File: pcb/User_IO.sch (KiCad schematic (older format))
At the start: 17 parts

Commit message: Added part numbers and updated schematic
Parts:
- gave numbers to parts that had none: 17
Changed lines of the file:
@@
 $EndDescr
 $Comp
-L XC7Axxt-FGG484 U?
+L XC7Axxt-FGG484 U401
 U 5 1 565FC0A5
 P 3400 3950
-F 0 "U?" H 2500 1350 60  0000 C CNN
+F 0 "U401" H 2500 1350 60  0000 C CNN
 F 1 "XC7Axxt-FGG484" H 2800 6550 60  0000 C CNN
 F 2 "" H 3400 4000 60  0000 C CNN
@@
 $EndComp
 $Comp
-L LED D?
+L LED D1201
 U 1 1 565FC0D4
 P 6800 1600
-F 0 "D?" H 6800 1700 50  0000 C CNN
+F 0 "D1201" H 6800 1700 50  0000 C CNN
 F 1 "LED" H 6800 1500 50  0000 C CNN
 F 2 "" H 6800 1600 60  0000 C CNN
@@
 $EndComp
 $Comp
-L LED D?
+L LED D1202
 U 1 1 565FC10C
 P 6800 1900
-F 0 "D?" H 6800 2000 50  0000 C CNN
+F 0 "D1202" H 6800 2000 50  0000 C CNN
 F 1 "LED" H 6800 1800 50  0000 C CNN
 F 2 "" H 6800 1900 60  0000 C CNN
@@
 $EndComp
 $Comp
-L LED D?
+L LED D1203
 U 1 1 565FC132
 P 6800 2200
-F 0 "D?" H 6800 2300 50  0000 C CNN
+F 0 "D1203" H 6800 2300 50  0000 C CNN
 F 1 "LED" H 6800 2100 50  0000 C CNN
 F 2 "" H 6800 2200 60  0000 C CNN
@@
 $EndComp
 $Comp
-L LED D?
+L LED D1204
 U 1 1 565FC15A
 P 6800 2500
-F 0 "D?" H 6800 2600 50  0000 C CNN
+F 0 "D1204" H 6800 2600 50  0000 C CNN
 F 1 "LED" H 6800 2400 50  0000 C CNN
 F 2 "" H 6800 2500 60  0000 C CNN
@@
 $EndComp
 $Comp
-L R R?
+L R R1201
 U 1 1 565FC21B
 P 6350 1600
-F 0 "R?" V 6430 1600 50  0000 C CNN
+F 0 "R1201" V 6430 1600 50  0000 C CNN
 F 1 "R" V 6350 1600 50  0000 C CNN
 F 2 "" V 6280 1600 30  0000 C CNN
@@
 $EndComp
 $Comp
-L R R?
+L R R1202
 U 1 1 565FC251
 P 6350 1900
-F 0 "R?" V 6430 1900 50  0000 C CNN
+F 0 "R1202" V 6430 1900 50  0000 C CNN
 F 1 "R" V 6350 1900 50  0000 C CNN
 F 2 "" V 6280 1900 30  0000 C CNN
@@
 $EndComp
 $Comp
-L R R?
+L R R1203
 U 1 1 565FC282
 P 6350 2200
-F 0 "R?" V 6430 2200 50  0000 C CNN
+F 0 "R1203" V 6430 2200 50  0000 C CNN
 F 1 "R" V 6350 2200 50  0000 C CNN
 F 2 "" V 6280 2200 30  0000 C CNN
@@
 $EndComp
 $Comp
-L R R?
+L R R1204
 U 1 1 565FC2C2
 P 6350 2500
-F 0 "R?" V 6430 2500 50  0000 C CNN
+F 0 "R1204" V 6430 2500 50  0000 C CNN
 F 1 "R" V 6350 2500 50  0000 C CNN
 F 2 "" V 6280 2500 30  0000 C CNN
@@
 $EndComp
 $Comp
-L GND #PWR?
+L GND #PWR1203
 U 1 1 565FC384
 P 7100 2600
-F 0 "#PWR?" H 7100 2350 50  0001 C CNN
+F 0 "#PWR1203" H 7100 2350 50  0001 C CNN
 F 1 "GND" H 7100 2450 50  0000 C CNN
 F 2 "" H 7100 2600 60  0000 C CNN
@@
 $EndComp
 $Comp
-L CONN_02X05 P?
+L CONN_02X05 P1201
 U 1 1 565FC541
 P 8050 3300
-F 0 "P?" H 8050 3600 50  0000 C CNN
+F 0 "P1201" H 8050 3600 50  0000 C CNN
 F 1 "CONN_02X05" H 8050 3000 50  0000 C CNN
 F 2 "" H 8050 2100 60  0000 C CNN
@@
 $EndComp
 $Comp
-L CONN_02X05 P?
+L CONN_02X05 P1202
 U 1 1 565FC5D6
 P 8050 4200
-F 0 "P?" H 8050 4500 50  0000 C CNN
+F 0 "P1202" H 8050 4500 50  0000 C CNN
 F 1 "CONN_02X05" H 8050 3900 50  0000 C CNN
 F 2 "" H 8050 3000 60  0000 C CNN
@@
 IO15
 $Comp
-L GND #PWR?
+L GND #PWR1206
 U 1 1 565FD605
 P 8500 3600
-F 0 "#PWR?" H 8500 3350 50  0001 C CNN
+F 0 "#PWR1206" H 8500 3350 50  0001 C CNN
 F 1 "GND" H 8500 3450 50  0000 C CNN
 F 2 "" H 8500 3600 60  0000 C CNN
@@
 $EndComp
 $Comp
-L GND #PWR?
+L GND #PWR1207
 U 1 1 565FD63A
 P 8500 4500
-F 0 "#PWR?" H 8500 4250 50  0001 C CNN
+F 0 "#PWR1207" H 8500 4250 50  0001 C CNN
 F 1 "GND" H 8500 4350 50  0000 C CNN
 F 2 "" H 8500 4500 60  0000 C CNN
@@
 $EndComp
 $Comp
-L +3V3 #PWR?
+L +3V3 #PWR1204
 U 1 1 565FD72A
 P 7600 3600
-F 0 "#PWR?" H 7600 3450 50  0001 C CNN
+F 0 "#PWR1204" H 7600 3450 50  0001 C CNN
 F 1 "+3V3" H 7600 3740 50  0000 C CNN
 F 2 "" H 7600 3600 60  0000 C CNN
@@
 $EndComp
 $Comp
-L +3V3 #PWR?
+L +3V3 #PWR1205
 U 1 1 565FD75F
 P 7600 4500
-F 0 "#PWR?" H 7600 4350 50  0001 C CNN
+F 0 "#PWR1205" H 7600 4350 50  0001 C CNN
 F 1 "+3V3" H 7600 4640 50  0000 C CNN
 F 2 "" H 7600 4500 60  0000 C CNN
@@
 	7600 4400 7600 4500
 $Comp
-L SW_PUSH SW?
+L SW_PUSH SW1202
 U 1 1 565FD8DE
 P 10300 3400
-F 0 "SW?" H 10450 3510 50  0000 C CNN
+F 0 "SW1202" H 10450 3510 50  0000 C CNN
 F 1 "SW_PUSH" H 10300 3320 50  0000 C CNN
 F 2 "" H 10300 3400 60  0000 C CNN
@@
 $EndComp
 $Comp
-L SW_PUSH SW?
+L SW_PUSH SW1201
 U 1 1 565FD92F
 P 10000 3400
-F 0 "SW?" H 10150 3510 50  0000 C CNN
+F 0 "SW1201" H 10150 3510 50  0000 C CNN
 F 1 "SW_PUSH" H 10000 3320 50  0000 C CNN
 F 2 "" H 10000 3400 60  0000 C CNN
@@
 $EndComp
 $Comp
-L R R?
+L R R1208
 U 1 1 565FD996
 P 10300 2750
-F 0 "R?" V 10380 2750 50  0000 C CNN
+F 0 "R1208" V 10380 2750 50  0000 C CNN
 F 1 "R" V 10300 2750 50  0000 C CNN
 F 2 "" V 10230 2750 30  0000 C CNN
@@
 $EndComp
 $Comp
-L R R?
+L R R1207
 U 1 1 565FD9E8
 P 10000 2750
-F 0 "R?" V 10080 2750 50  0000 C CNN
+F 0 "R1207" V 10080 2750 50  0000 C CNN
 F 1 "R" V 10000 2750 50  0000 C CNN
 F 2 "" V 9930 2750 30  0000 C CNN
@@
 $EndComp
 $Comp
-L +3V3 #PWR?
+L +3V3 #PWR1208
 U 1 1 565FDB4D
 P 10000 2400
-F 0 "#PWR?" H 10000 2250 50  0001 C CNN
+F 0 "#PWR1208" H 10000 2250 50  0001 C CNN
 F 1 "+3V3" H 10000 2540 50  0000 C CNN
 F 2 "" H 10000 2400 60  0000 C CNN
@@
 $EndComp
 $Comp
-L GND #PWR?
+L GND #PWR1209
 U 1 1 565FDBBB
 P 10000 3900
-F 0 "#PWR?" H 10000 3650 50  0001 C CNN
+F 0 "#PWR1209" H 10000 3650 50  0001 C CNN
 F 1 "GND" H 10000 3750 50  0000 C CNN
 F 2 "" H 10000 3900 60  0000 C CNN
@@
 SFP_SCL
 $Comp
-L R R?
+L R R1205
 U 1 1 566081C8
 P 6500 4950
-F 0 "R?" V 6580 4950 50  0000 C CNN
+F 0 "R1205" V 6580 4950 50  0000 C CNN
 F 1 "R" V 6500 4950 50  0000 C CNN
 F 2 "" V 6430 4950 30  0000 C CNN
@@
 $EndComp
 $Comp
-L R R?
+L R R1206
 U 1 1 5660821E
 P 6500 5750
-F 0 "R?" V 6580 5750 50  0000 C CNN
+F 0 "R1206" V 6580 5750 50  0000 C CNN
 F 1 "R" V 6500 5750 50  0000 C CNN
 F 2 "" V 6430 5750 30  0000 C CNN
@@
 $EndComp
 $Comp
-L +3V3 #PWR?
+L +3V3 #PWR1201
 U 1 1 56608307
 P 6500 4700
-F 0 "#PWR?" H 6500 4550 50  0001 C CNN
+F 0 "#PWR1201" H 6500 4550 50  0001 C CNN
 F 1 "+3V3" H 6500 4840 50  0000 C CNN
 F 2 "" H 6500 4700 60  0000 C CNN
@@
 $EndComp
 $Comp
-L +3V3 #PWR?
+L +3V3 #PWR1202
 U 1 1 5660834E
 P 6500 5500
-F 0 "#PWR?" H 6500 5350 50  0001 C CNN
+F 0 "#PWR1202" H 6500 5350 50  0001 C CNN
 F 1 "+3V3" H 6500 5640 50  0000 C CNN
 F 2 "" H 6500 5500 60  0000 C CNN

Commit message: mostly done with component placement
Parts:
- D1201, D1202, D1203, D1204: footprint (none) -> LEDs:LED-0805
- P1201, P1202: footprint (none) -> Pin_Headers:Pin_Header_Straight_2x05
- R1201, R1202, R1203, R1204, R1205, R1206, R1207, R1208: footprint (none) -> wbraun_smd:R_0402
- SW1201, SW1202: footprint (none) -> wbraun_smd:button-5mm
- U401: footprint (none) -> wbraun_smd:BGA_484_22x22_FULLARRAY_1MM
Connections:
- net +3V3: now also R1206.1
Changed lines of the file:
@@
 F 0 "U401" H 2500 1350 60  0000 C CNN
 F 1 "XC7Axxt-FGG484" H 2800 6550 60  0000 C CNN
-F 2 "" H 3400 4000 60  0000 C CNN
+F 2 "wbraun_smd:BGA_484_22x22_FULLARRAY_1MM" H 3400 4000 60  0001 C CNN
 F 3 "" H 3400 4000 60  0000 C CNN
 	5    3400 3950
@@
 F 0 "D1201" H 6800 1700 50  0000 C CNN
 F 1 "LED" H 6800 1500 50  0000 C CNN
-F 2 "" H 6800 1600 60  0000 C CNN
+F 2 "LEDs:LED-0805" H 6800 1600 60  0001 C CNN
 F 3 "" H 6800 1600 60  0000 C CNN
 	1    6800 1600
@@
 F 0 "D1202" H 6800 2000 50  0000 C CNN
 F 1 "LED" H 6800 1800 50  0000 C CNN
-F 2 "" H 6800 1900 60  0000 C CNN
+F 2 "LEDs:LED-0805" H 6800 1900 60  0001 C CNN
 F 3 "" H 6800 1900 60  0000 C CNN
 	1    6800 1900
@@
 F 0 "D1203" H 6800 2300 50  0000 C CNN
 F 1 "LED" H 6800 2100 50  0000 C CNN
-F 2 "" H 6800 2200 60  0000 C CNN
+F 2 "LEDs:LED-0805" H 6800 2200 60  0001 C CNN
 F 3 "" H 6800 2200 60  0000 C CNN
 	1    6800 2200
@@
 F 0 "D1204" H 6800 2600 50  0000 C CNN
 F 1 "LED" H 6800 2400 50  0000 C CNN
-F 2 "" H 6800 2500 60  0000 C CNN
+F 2 "LEDs:LED-0805" H 6800 2500 60  0001 C CNN
 F 3 "" H 6800 2500 60  0000 C CNN
 	1    6800 2500
@@
 F 0 "R1201" V 6430 1600 50  0000 C CNN
 F 1 "R" V 6350 1600 50  0000 C CNN
-F 2 "" V 6280 1600 30  0000 C CNN
+F 2 "wbraun_smd:R_0402" V 6280 1600 30  0001 C CNN
 F 3 "" H 6350 1600 30  0000 C CNN
 	1    6350 1600
@@
 F 0 "R1202" V 6430 1900 50  0000 C CNN
 F 1 "R" V 6350 1900 50  0000 C CNN
-F 2 "" V 6280 1900 30  0000 C CNN
+F 2 "wbraun_smd:R_0402" V 6280 1900 30  0001 C CNN
 F 3 "" H 6350 1900 30  0000 C CNN
 	1    6350 1900
@@
 F 0 "R1203" V 6430 2200 50  0000 C CNN
 F 1 "R" V 6350 2200 50  0000 C CNN
-F 2 "" V 6280 2200 30  0000 C CNN
+F 2 "wbraun_smd:R_0402" V 6280 2200 30  0001 C CNN
 F 3 "" H 6350 2200 30  0000 C CNN
 	1    6350 2200
@@
 F 0 "R1204" V 6430 2500 50  0000 C CNN
 F 1 "R" V 6350 2500 50  0000 C CNN
-F 2 "" V 6280 2500 30  0000 C CNN
+F 2 "wbraun_smd:R_0402" V 6280 2500 30  0001 C CNN
 F 3 "" H 6350 2500 30  0000 C CNN
 	1    6350 2500
@@
 $EndComp
 $Comp
-L GND #PWR1203
+L GND #PWR0165
 U 1 1 565FC384
 P 7100 2600
-F 0 "#PWR1203" H 7100 2350 50  0001 C CNN
+F 0 "#PWR0165" H 7100 2350 50  0001 C CNN
 F 1 "GND" H 7100 2450 50  0000 C CNN
 F 2 "" H 7100 2600 60  0000 C CNN
@@
 F 0 "P1201" H 8050 3600 50  0000 C CNN
 F 1 "CONN_02X05" H 8050 3000 50  0000 C CNN
-F 2 "" H 8050 2100 60  0000 C CNN
+F 2 "Pin_Headers:Pin_Header_Straight_2x05" H 8050 2100 60  0001 C CNN
 F 3 "" H 8050 2100 60  0000 C CNN
 	1    8050 3300
@@
 F 0 "P1202" H 8050 4500 50  0000 C CNN
 F 1 "CONN_02X05" H 8050 3900 50  0000 C CNN
-F 2 "" H 8050 3000 60  0000 C CNN
+F 2 "Pin_Headers:Pin_Header_Straight_2x05" H 8050 3000 60  0001 C CNN
 F 3 "" H 8050 3000 60  0000 C CNN
 	1    8050 4200
@@
 IO15
 $Comp
-L GND #PWR1206
+L GND #PWR0166
 U 1 1 565FD605
 P 8500 3600
-F 0 "#PWR1206" H 8500 3350 50  0001 C CNN
+F 0 "#PWR0166" H 8500 3350 50  0001 C CNN
 F 1 "GND" H 8500 3450 50  0000 C CNN
 F 2 "" H 8500 3600 60  0000 C CNN
@@
 $EndComp
 $Comp
-L GND #PWR1207
+L GND #PWR0167
 U 1 1 565FD63A
 P 8500 4500
-F 0 "#PWR1207" H 8500 4250 50  0001 C CNN
+F 0 "#PWR0167" H 8500 4250 50  0001 C CNN
 F 1 "GND" H 8500 4350 50  0000 C CNN
 F 2 "" H 8500 4500 60  0000 C CNN
@@
 $EndComp
 $Comp
-L +3V3 #PWR1204
+L +3V3 #PWR0168
 U 1 1 565FD72A
 P 7600 3600
-F 0 "#PWR1204" H 7600 3450 50  0001 C CNN
+F 0 "#PWR0168" H 7600 3450 50  0001 C CNN
 F 1 "+3V3" H 7600 3740 50  0000 C CNN
 F 2 "" H 7600 3600 60  0000 C CNN
@@
 $EndComp
 $Comp
-L +3V3 #PWR1205
+L +3V3 #PWR0169
 U 1 1 565FD75F
 P 7600 4500
-F 0 "#PWR1205" H 7600 4350 50  0001 C CNN
+F 0 "#PWR0169" H 7600 4350 50  0001 C CNN
 F 1 "+3V3" H 7600 4640 50  0000 C CNN
 F 2 "" H 7600 4500 60  0000 C CNN
@@
 F 0 "SW1202" H 10450 3510 50  0000 C CNN
 F 1 "SW_PUSH" H 10300 3320 50  0000 C CNN
-F 2 "" H 10300 3400 60  0000 C CNN
+F 2 "wbraun_smd:button-5mm" H 10300 3400 60  0001 C CNN
 F 3 "" H 10300 3400 60  0000 C CNN
 	1    10300 3400
@@
 F 0 "SW1201" H 10150 3510 50  0000 C CNN
 F 1 "SW_PUSH" H 10000 3320 50  0000 C CNN
-F 2 "" H 10000 3400 60  0000 C CNN
+F 2 "wbraun_smd:button-5mm" H 10000 3400 60  0001 C CNN
 F 3 "" H 10000 3400 60  0000 C CNN
 	1    10000 3400
@@
 F 0 "R1208" V 10380 2750 50  0000 C CNN
 F 1 "R" V 10300 2750 50  0000 C CNN
-F 2 "" V 10230 2750 30  0000 C CNN
+F 2 "wbraun_smd:R_0402" V 10230 2750 30  0001 C CNN
 F 3 "" H 10300 2750 30  0000 C CNN
 	1    10300 2750
@@
 F 0 "R1207" V 10080 2750 50  0000 C CNN
 F 1 "R" V 10000 2750 50  0000 C CNN
-F 2 "" V 9930 2750 30  0000 C CNN
+F 2 "wbraun_smd:R_0402" V 9930 2750 30  0001 C CNN
 F 3 "" H 10000 2750 30  0000 C CNN
 	1    10000 2750
@@
 $EndComp
 $Comp
-L +3V3 #PWR1208
+L +3V3 #PWR0170
 U 1 1 565FDB4D
 P 10000 2400
-F 0 "#PWR1208" H 10000 2250 50  0001 C CNN
+F 0 "#PWR0170" H 10000 2250 50  0001 C CNN
 F 1 "+3V3" H 10000 2540 50  0000 C CNN
 F 2 "" H 10000 2400 60  0000 C CNN
@@
 $EndComp
 $Comp
-L GND #PWR1209
+L GND #PWR0171
 U 1 1 565FDBBB
 P 10000 3900
-F 0 "#PWR1209" H 10000 3650 50  0001 C CNN
+F 0 "#PWR0171" H 10000 3650 50  0001 C CNN
 F 1 "GND" H 10000 3750 50  0000 C CNN
 F 2 "" H 10000 3900 60  0000 C CNN
@@
 F 0 "R1205" V 6580 4950 50  0000 C CNN
 F 1 "R" V 6500 4950 50  0000 C CNN
-F 2 "" V 6430 4950 30  0000 C CNN
+F 2 "wbraun_smd:R_0402" V 6430 4950 30  0001 C CNN
 F 3 "" H 6500 4950 30  0000 C CNN
 	1    6500 4950
@@
 F 0 "R1206" V 6580 5750 50  0000 C CNN
 F 1 "R" V 6500 5750 50  0000 C CNN
-F 2 "" V 6430 5750 30  0000 C CNN
+F 2 "wbraun_smd:R_0402" V 6430 5750 30  0001 C CNN
 F 3 "" H 6500 5750 30  0000 C CNN
 	1    6500 5750
@@
 $EndComp
 $Comp
-L +3V3 #PWR1201
+L +3V3 #PWR0172
 U 1 1 56608307
 P 6500 4700
-F 0 "#PWR1201" H 6500 4550 50  0001 C CNN
+F 0 "#PWR0172" H 6500 4550 50  0001 C CNN
 F 1 "+3V3" H 6500 4840 50  0000 C CNN
 F 2 "" H 6500 4700 60  0000 C CNN
@@
 $EndComp
 $Comp
-L +3V3 #PWR1202
+L +3V3 #PWR0173
 U 1 1 5660834E
 P 6500 5500
-F 0 "#PWR1202" H 6500 5350 50  0001 C CNN
+F 0 "#PWR0173" H 6500 5350 50  0001 C CNN
 F 1 "+3V3" H 6500 5640 50  0000 C CNN
 F 2 "" H 6500 5500 60  0000 C CNN
@@
 Text HLabel 8100 5900 2    60   Input ~ 0
 PCIE_PERST
+Wire Wire Line
+	6500 5500 6500 5600
 $EndSCHEMATC

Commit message: Finished initial component placement
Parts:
- removed R1205, R1206: R, wbraun_smd:R_0402, symbol R
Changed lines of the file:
@@
 Text Label 4700 5500 0    60   ~ 0
 SFP_SCL
-$Comp
-L R R1205
-U 1 1 566081C8
-P 6500 4950
-F 0 "R1205" V 6580 4950 50  0000 C CNN
-F 1 "R" V 6500 4950 50  0000 C CNN
-F 2 "wbraun_smd:R_0402" V 6430 4950 30  0001 C CNN
-F 3 "" H 6500 4950 30  0000 C CNN
-	1    6500 4950
-	1    0    0    -1
-$EndComp
-$Comp
-L R R1206
-U 1 1 5660821E
-P 6500 5750
-F 0 "R1206" V 6580 5750 50  0000 C CNN
-F 1 "R" V 6500 5750 50  0000 C CNN
-F 2 "wbraun_smd:R_0402" V 6430 5750 30  0001 C CNN
-F 3 "" H 6500 5750 30  0000 C CNN
-	1    6500 5750
-	1    0    0    -1
-$EndComp
-$Comp
-L +3V3 #PWR0172
-U 1 1 56608307
-P 6500 4700
-F 0 "#PWR0172" H 6500 4550 50  0001 C CNN
-F 1 "+3V3" H 6500 4840 50  0000 C CNN
-F 2 "" H 6500 4700 60  0000 C CNN
-F 3 "" H 6500 4700 60  0000 C CNN
-	1    6500 4700
-	1    0    0    -1
-$EndComp
-$Comp
-L +3V3 #PWR0173
-U 1 1 5660834E
-P 6500 5500
-F 0 "#PWR0173" H 6500 5350 50  0001 C CNN
-F 1 "+3V3" H 6500 5640 50  0000 C CNN
-F 2 "" H 6500 5500 60  0000 C CNN
-F 3 "" H 6500 5500 60  0000 C CNN
-	1    6500 5500
-	1    0    0    -1
-$EndComp
-Wire Wire Line
-	6500 4700 6500 4800
-Wire Wire Line
-	6300 5100 6700 5100
-Connection ~ 6500 5100
-Wire Wire Line
-	6300 5900 6700 5900
-Connection ~ 6500 5900
 Wire Wire Line
 	7700 5300 8100 5300
@@
 PCIE_PERST
 Wire Wire Line
-	6500 5500 6500 5600
+	6300 5100 6700 5100
+Wire Wire Line
+	6300 5900 6700 5900
 $EndSCHEMATC

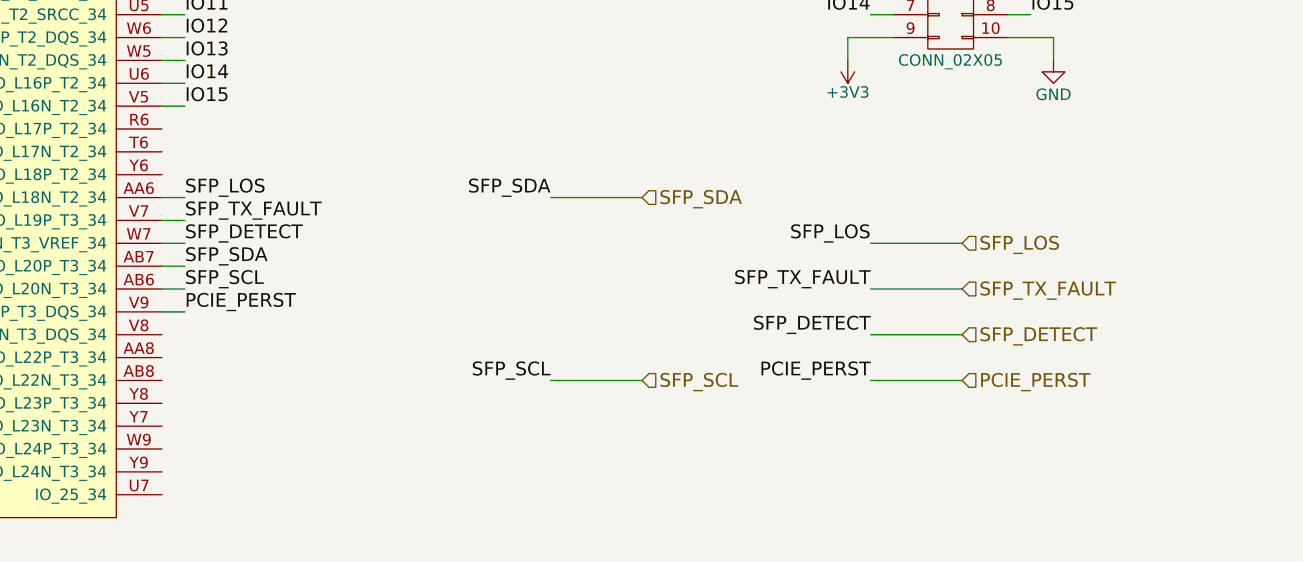
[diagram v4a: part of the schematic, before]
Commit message: Finished most of the routing, removed DDR-3
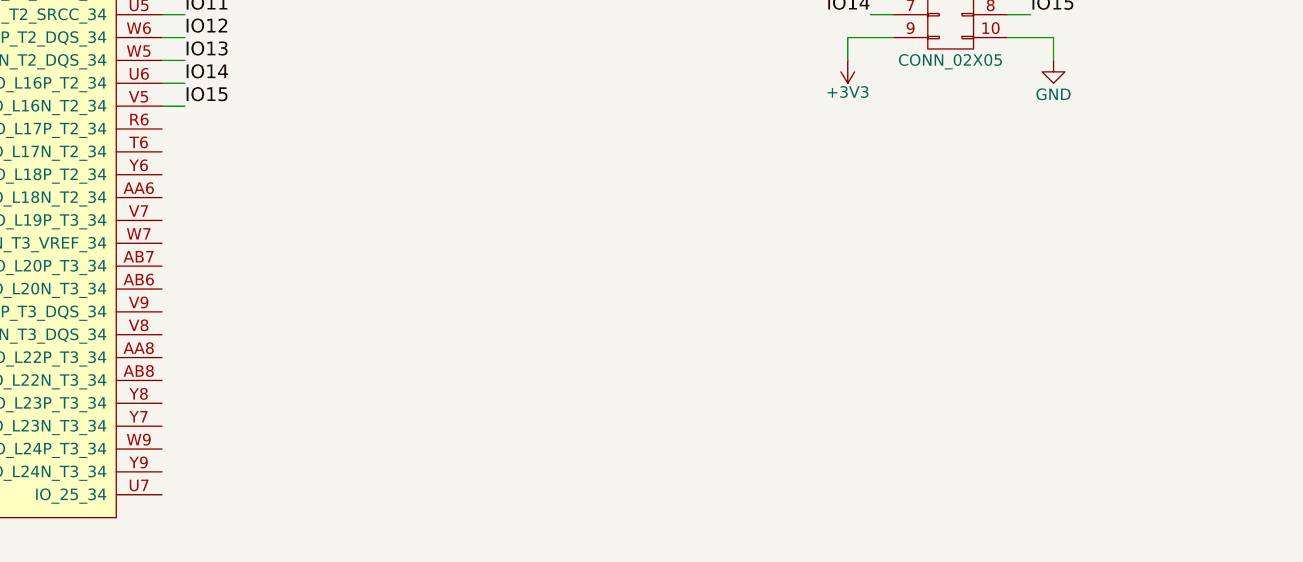
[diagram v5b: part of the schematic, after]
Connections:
- net PCIE_PERST: no longer names the net of U401.V9 (IO_L21P_T3_DQS_34)
- net SFP_DETECT: no longer names the net of U401.W7 (IO_L19N_T3_VREF_34)
- net SFP_LOS: no longer names the net of U401.AA6 (IO_L18N_T2_34)
- net SFP_SCL: no longer names the net of U401.AB6 (IO_L20N_T3_34)
- net SFP_SDA: no longer names the net of U401.AB7 (IO_L20P_T3_34)
- net SFP_TX_FAULT: no longer names the net of U401.V7 (IO_L19P_T3_34)
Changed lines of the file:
@@
 $Descr A4 11693 8268
 encoding utf-8
-Sheet 12 13
+Sheet 12 11
 Title ""
 Date ""
@@
 $EndComp
 $Comp
-L GND #PWR0165
+L GND #PWR0156
 U 1 1 565FC384
 P 7100 2600
-F 0 "#PWR0165" H 7100 2350 50  0001 C CNN
+F 0 "#PWR0156" H 7100 2350 50  0001 C CNN
 F 1 "GND" H 7100 2450 50  0000 C CNN
 F 2 "" H 7100 2600 60  0000 C CNN
@@
 IO15
 $Comp
-L GND #PWR0166
+L GND #PWR0157
 U 1 1 565FD605
 P 8500 3600
-F 0 "#PWR0166" H 8500 3350 50  0001 C CNN
+F 0 "#PWR0157" H 8500 3350 50  0001 C CNN
 F 1 "GND" H 8500 3450 50  0000 C CNN
 F 2 "" H 8500 3600 60  0000 C CNN
@@
 $EndComp
 $Comp
-L GND #PWR0167
+L GND #PWR0158
 U 1 1 565FD63A
 P 8500 4500
-F 0 "#PWR0167" H 8500 4250 50  0001 C CNN
+F 0 "#PWR0158" H 8500 4250 50  0001 C CNN
 F 1 "GND" H 8500 4350 50  0000 C CNN
 F 2 "" H 8500 4500 60  0000 C CNN
@@
 $EndComp
 $Comp
-L +3V3 #PWR0168
+L +3V3 #PWR0159
 U 1 1 565FD72A
 P 7600 3600
-F 0 "#PWR0168" H 7600 3450 50  0001 C CNN
+F 0 "#PWR0159" H 7600 3450 50  0001 C CNN
 F 1 "+3V3" H 7600 3740 50  0000 C CNN
 F 2 "" H 7600 3600 60  0000 C CNN
@@
 $EndComp
 $Comp
-L +3V3 #PWR0169
+L +3V3 #PWR0160
 U 1 1 565FD75F
 P 7600 4500
-F 0 "#PWR0169" H 7600 4350 50  0001 C CNN
+F 0 "#PWR0160" H 7600 4350 50  0001 C CNN
 F 1 "+3V3" H 7600 4640 50  0000 C CNN
 F 2 "" H 7600 4500 60  0000 C CNN
@@
 $EndComp
 $Comp
-L +3V3 #PWR0170
+L +3V3 #PWR0161
 U 1 1 565FDB4D
 P 10000 2400
-F 0 "#PWR0170" H 10000 2250 50  0001 C CNN
+F 0 "#PWR0161" H 10000 2250 50  0001 C CNN
 F 1 "+3V3" H 10000 2540 50  0000 C CNN
 F 2 "" H 10000 2400 60  0000 C CNN
@@
 $EndComp
 $Comp
-L GND #PWR0171
+L GND #PWR0162
 U 1 1 565FDBBB
 P 10000 3900
-F 0 "#PWR0171" H 10000 3650 50  0001 C CNN
+F 0 "#PWR0162" H 10000 3650 50  0001 C CNN
 F 1 "GND" H 10000 3750 50  0000 C CNN
 F 2 "" H 10000 3900 60  0000 C CNN
@@
 Text Label 9800 3100 2    60   ~ 0
 B1
-Wire Wire Line
-	4600 5100 4700 5100
-Wire Wire Line
-	4600 5200 4700 5200
-Wire Wire Line
-	4600 5300 4700 5300
-Text Label 4700 5100 0    60   ~ 0
-SFP_LOS
-Text Label 4700 5200 0    60   ~ 0
-SFP_TX_FAULT
-Text Label 4700 5300 0    60   ~ 0
-SFP_DETECT
-Wire Wire Line
-	4600 5400 4700 5400
-Wire Wire Line
-	4600 5500 4700 5500
-Text Label 4700 5400 0    60   ~ 0
-SFP_SDA
-Text Label 4700 5500 0    60   ~ 0
-SFP_SCL
-Wire Wire Line
-	7700 5300 8100 5300
-Wire Wire Line
-	7700 5500 8100 5500
-Wire Wire Line
-	7700 5700 8100 5700
-Text Label 6300 5100 2    60   ~ 0
-SFP_SDA
-Text Label 6300 5900 2    60   ~ 0
-SFP_SCL
-Text Label 7700 5300 2    60   ~ 0
-SFP_LOS
-Text Label 7700 5500 2    60   ~ 0
-SFP_TX_FAULT
-Text Label 7700 5700 2    60   ~ 0
-SFP_DETECT
-Text HLabel 6700 5100 2    60   Input ~ 0
-SFP_SDA
-Text HLabel 6700 5900 2    60   Input ~ 0
-SFP_SCL
-Text HLabel 8100 5300 2    60   Input ~ 0
-SFP_LOS
-Text HLabel 8100 5500 2    60   Input ~ 0
-SFP_TX_FAULT
-Text HLabel 8100 5700 2    60   Input ~ 0
-SFP_DETECT
-Wire Wire Line
-	4600 5600 4700 5600
-Text Label 4700 5600 0    60   ~ 0
-PCIE_PERST
-Wire Wire Line
-	7700 5900 8100 5900
-Text Label 7700 5900 2    60   ~ 0
-PCIE_PERST
-Text HLabel 8100 5900 2    60   Input ~ 0
-PCIE_PERST
-Wire Wire Line
-	6300 5100 6700 5100
-Wire Wire Line
-	6300 5900 6700 5900
 $EndSCHEMATC
